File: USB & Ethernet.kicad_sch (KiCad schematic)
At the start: 1 part

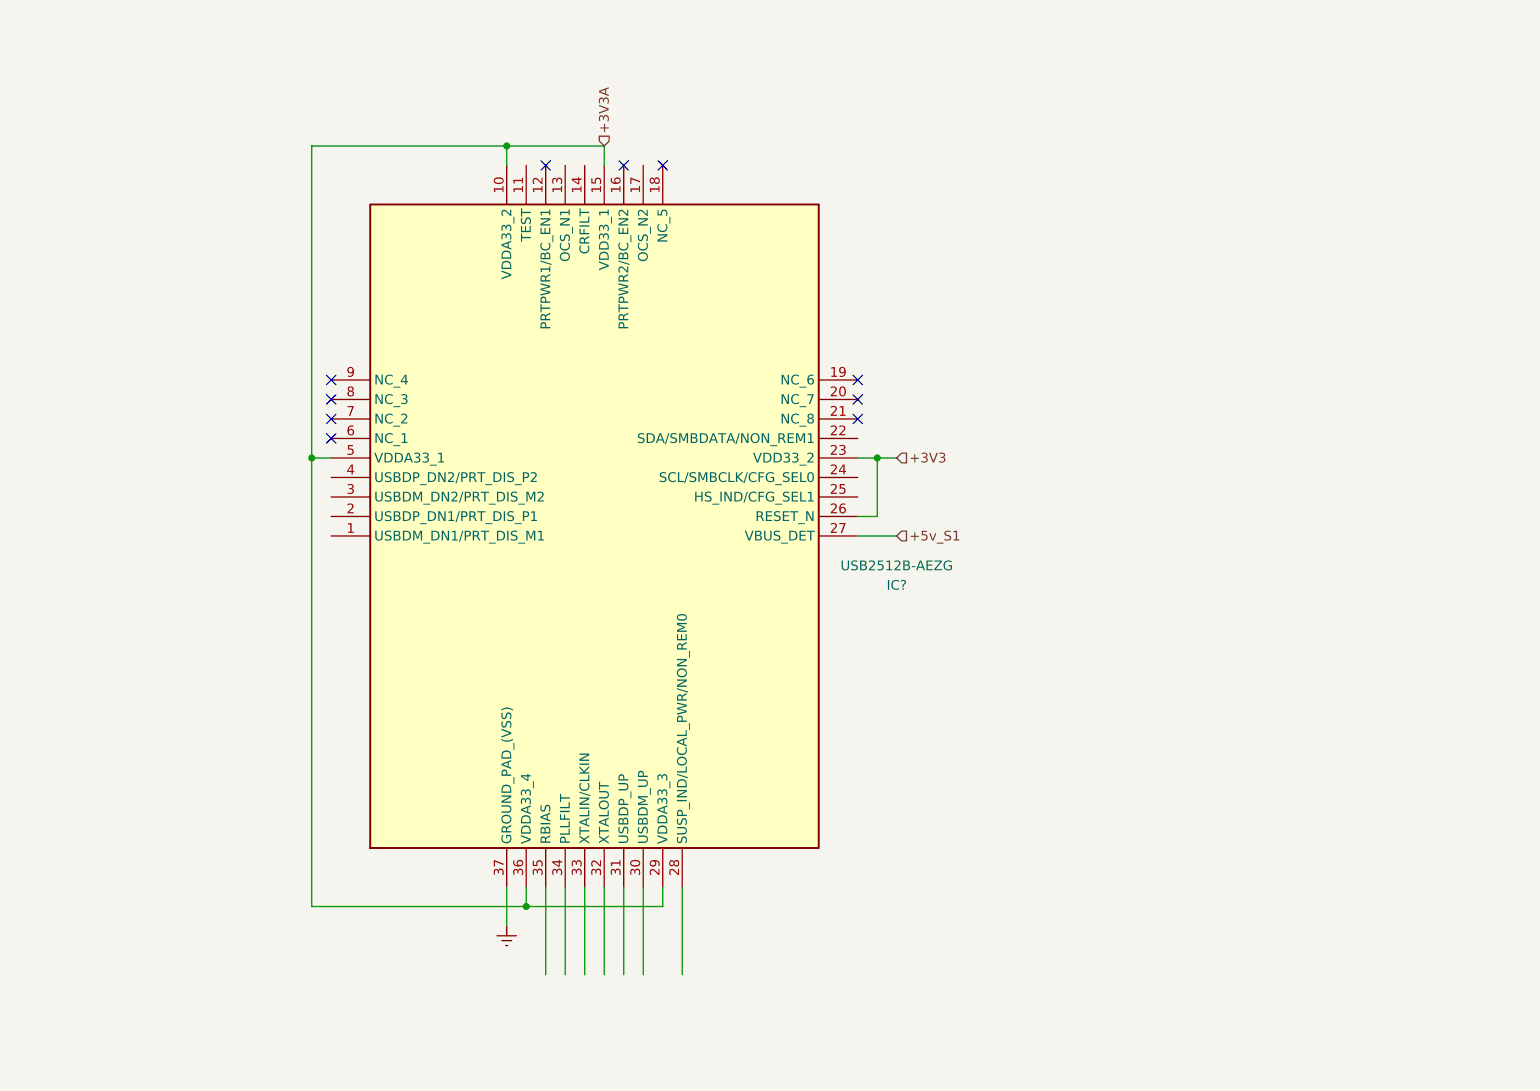
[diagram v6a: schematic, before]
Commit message: More Fans
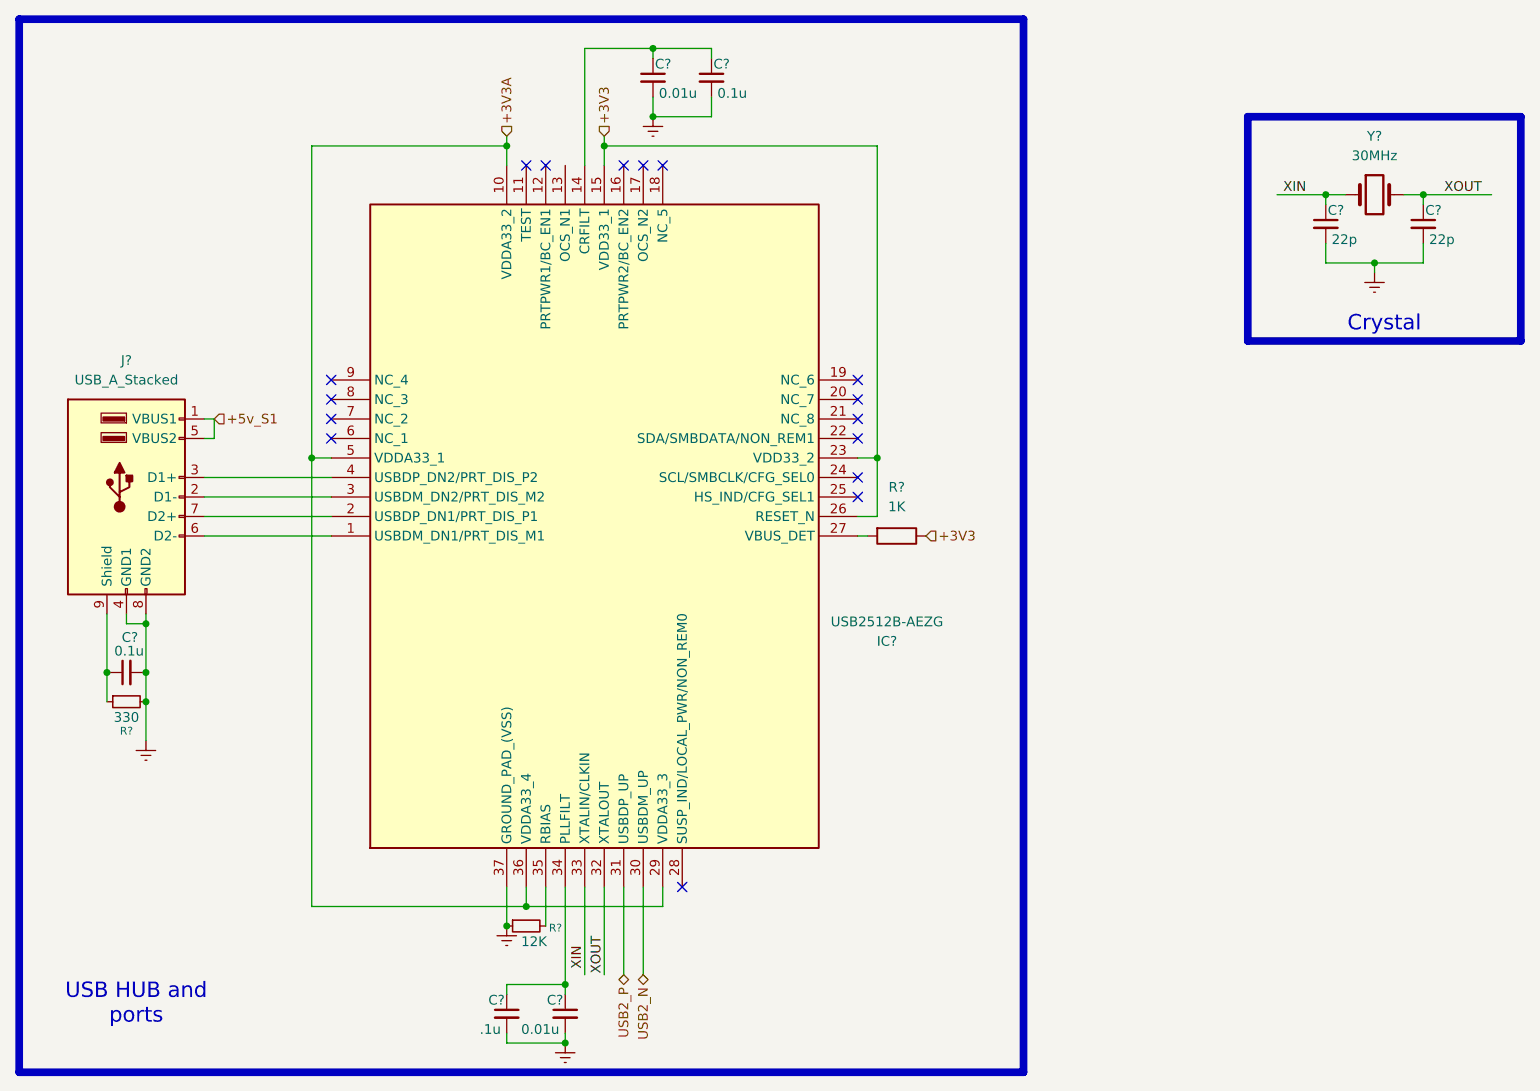
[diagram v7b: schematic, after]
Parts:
- added C? (x2): 0.01u, symbol Device:C_Small
- added C?: .1u, symbol Device:C_Small
- added C? (x2): 22p, symbol Device:C_Small
- added C? (x2): 0.1u, symbol Device:C_Small
- added J?: USB_A_Stacked, symbol Connector:USB_A_Stacked
- added R?: 330, symbol Device:R_Small
- added R?: 12K, symbol Device:R_Small
- added R?: 1K, symbol Device:R
- added Y?: 30MHz, symbol Device:Crystal
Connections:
- net +3V3: now also IC?.15 (VDD33_1), R?.1
- net +3V3A: no longer IC?.15 (VDD33_1)
- net +5v_S1: now also J?.1 (VBUS1), J?.5 (VBUS2); no longer IC?.27 (VBUS_DET)
- net at IC?.1 (USBDM_DN1/PRT_DIS_M1): now also J?.6 (D2-)
- net at IC?.14 (CRFILT): now also C?.1, C?.1
- net at IC?.2 (USBDP_DN1/PRT_DIS_P1): now also J?.7 (D2+)
- net at IC?.3 (USBDM_DN2/PRT_DIS_M2): now also J?.2 (D1-)
- net USB2_N: now reaches IC?.30 (USBDM_UP)
- net USB2_P: now reaches IC?.31 (USBDP_UP)
- net XOUT: now reaches IC?.32 (XTALOUT)
- net XOUT: now also C?.1, Y?.2
- net XIN: now reaches IC?.33 (XTALIN/CLKIN)
- net XIN: now also C?.1, Y?.1
- net at IC?.34 (PLLFILT): now also C?.1, C?.1
- net at IC?.35 (RBIAS): now also R?.2
- net at IC?.37 (GROUND_PAD_(VSS)): now also R?.1
- net at IC?.4 (USBDP_DN2/PRT_DIS_P2): now also J?.3 (D1+)
- new net: IC?.27 (VBUS_DET), R?.2
- new net: C?.2, C?.2 (x3)
- new net: C?.2, J?.4 (GND1), J?.8 (GND2), R?.2
- new net: C?.1, J?.9 (Shield), R?.1
- no-connect marks 10 -> 16
